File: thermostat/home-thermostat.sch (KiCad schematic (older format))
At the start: 35 parts, among them J1 SMA, SW1 SW_Push, U1 MKW41Z512VHT, Y1 32MHz, Y2 32,768KHz

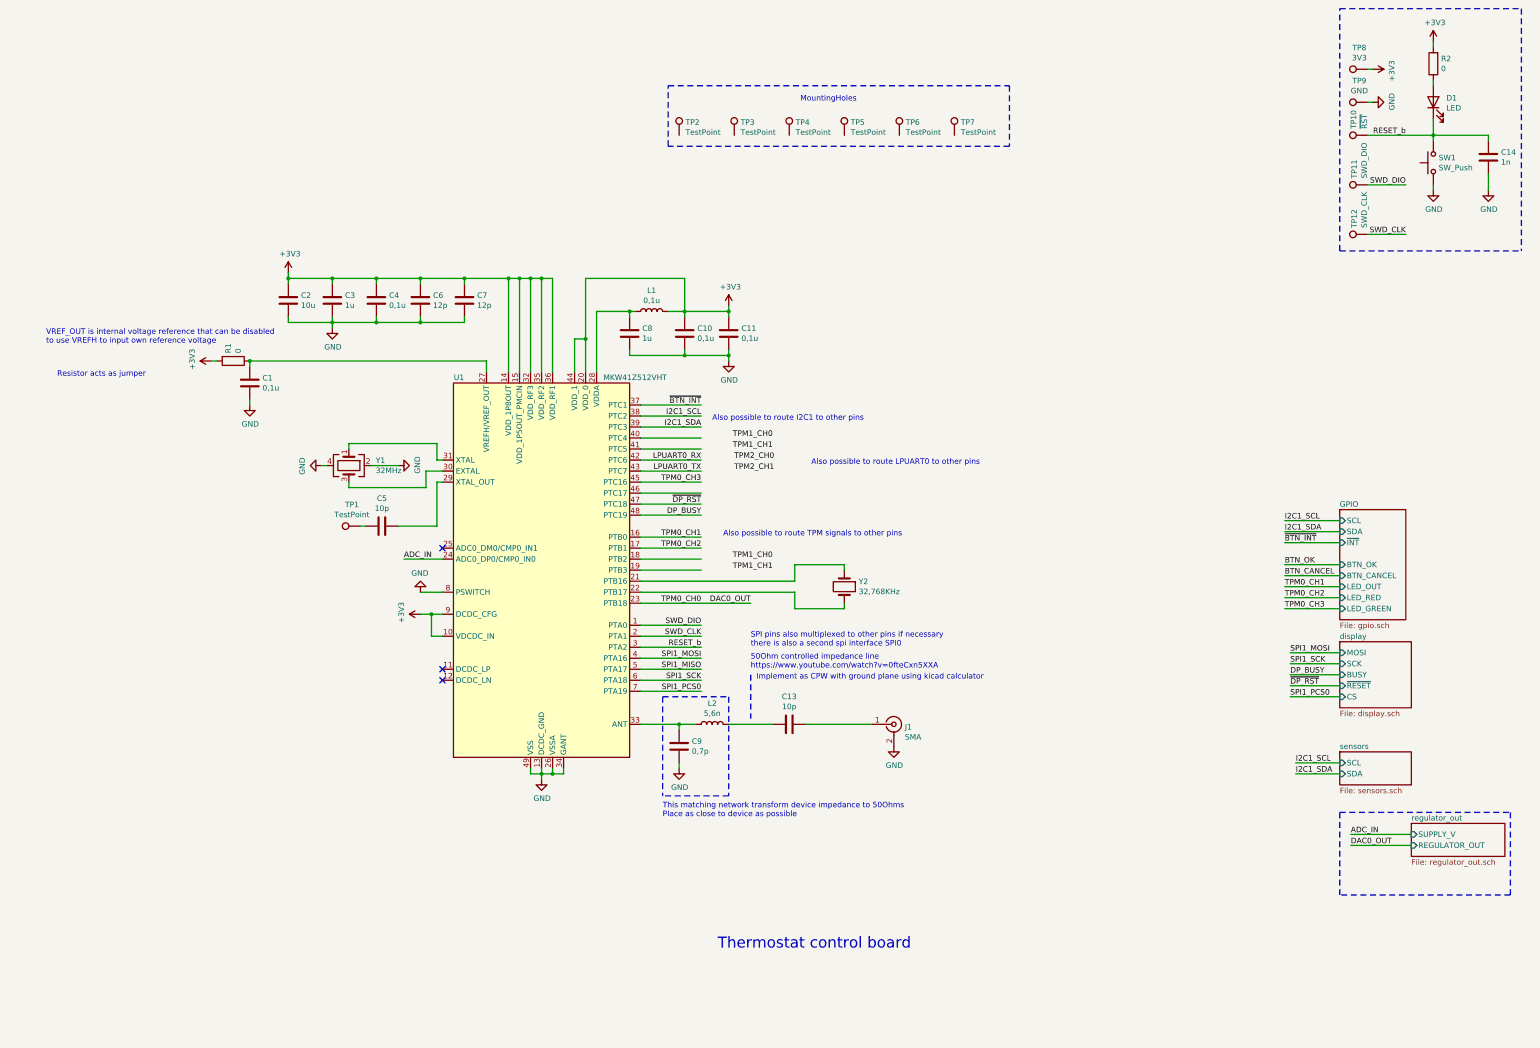
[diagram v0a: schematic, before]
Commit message: Finalized Thermostat circuit based on the MKW41Z.
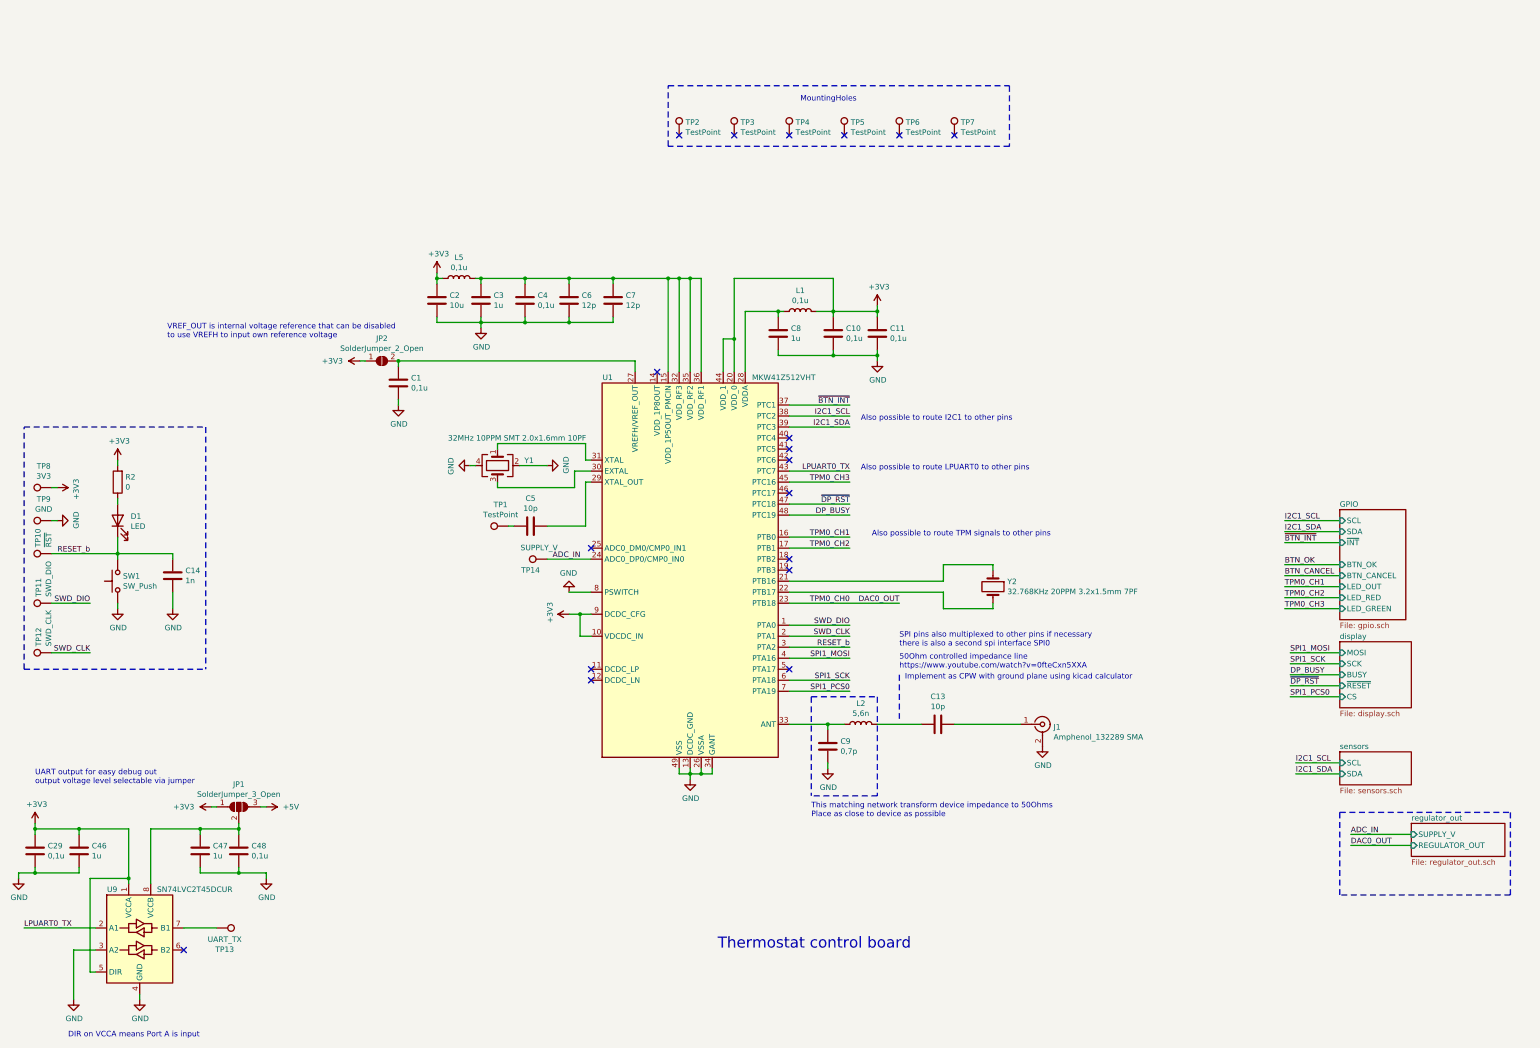
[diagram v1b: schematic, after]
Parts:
- removed R1: 0, Resistor_SMD:R_0603_1608Metric, symbol Device:R
- added C29, C48: 0,1u, Capacitor_SMD:C_0603_1608Metric, symbol Device:C
- added C46, C47: 1u, Capacitor_SMD:C_0603_1608Metric, symbol Device:C
- added JP1: SolderJumper_3_Open, Jumper:SolderJumper-3_P1.3mm_Open_Pad1.0x1.5mm, symbol Jumper:SolderJumper_3_Open
- added JP2: SolderJumper_2_Open, Jumper:SolderJumper-2_P1.3mm_Open_Pad1.0x1.5mm, symbol Jumper:SolderJumper_2_Open
- added L5: 0,1u, Inductor_SMD:L_0402_1005Metric, symbol Device:L
- added TP13: UART_TX, TestPoint:TestPoint_Pad_D1.0mm, symbol Connector:TestPoint
- added TP14: SUPPLY_V, TestPoint:TestPoint_Pad_D1.0mm, symbol Connector:TestPoint
- added U9: SN74LVC2T45DCUR, Package_SO:VSSOP-8_2.4x2.1mm_P0.5mm, symbol Logic_LevelTranslator:SN74LVC2T45DCUR
- C1, C10, C11, C13, C3, C4, C5, C6, C7, C9: footprint (none) -> Capacitor_SMD:C_0402_1005Metric
- C2, C8: footprint (none) -> Capacitor_SMD:C_0603_1608Metric
- J1: value SMA -> Amphenol_132289 SMA; footprint (none) -> Connector_Coaxial:SMA_Amphenol_132289_EdgeMount
- L1, L2: footprint (none) -> Inductor_SMD:L_0402_1005Metric
- U1: footprint Package_DFN_QFN:NXP_VQFN-48-1EP_7x7mm_P0.5mm_EP3.5x3.5mm_16xMask0.45x0.45_ThermalVias -> Package_DFN_QFN:NXP_LQFN-48-1EP_7x7mm_P0.5mm_EP3.5x3.5mm_16xMask0.45x0.45_ThermalVias
- Y1: value 32MHz -> 32MHz 10PPM SMT 2.0x1.6mm 10PF; footprint (none) -> Crystal:Crystal_SMD_2016-4Pin_2.0x1.6mm
- Y2: value 32,768KHz -> 32.768KHz 20PPM 3.2x1.5mm 7PF; footprint (none) -> Crystal:Crystal_SMD_3215-2Pin_3.2x1.5mm
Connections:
- net labels added: +5V
- net labels removed: LPUART0_RX, SPI1_MISO, TPM1_CH0, TPM1_CH1, TPM2_CH0, TPM2_CH1
- wire segments 151 -> 176
- no-connect marks 3 -> 18
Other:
- note added: "DIR on VCCA means Port A is input\n"
- note added: "UART output for easy debug out\noutput voltage level selectable via jumper"
- note removed: "Resistor acts as jumper"
- moved on the sheet: C1, C10, C11, C13, C14, C2, C3, C4, C5, C6, C7, C8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

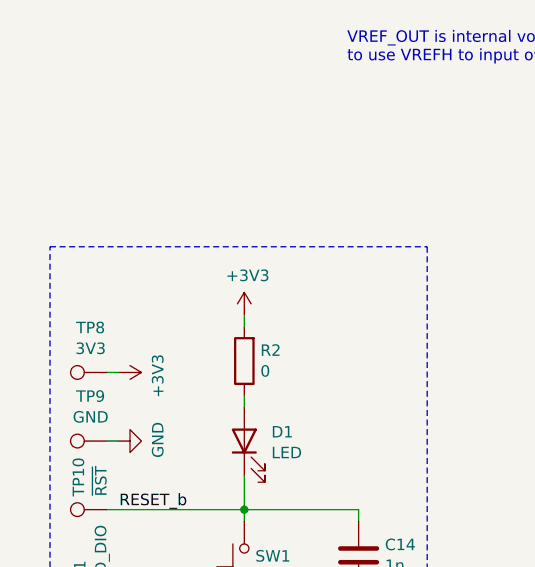
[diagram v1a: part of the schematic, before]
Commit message: Added testpad to supply rail +5V to allow flexible powering of board,also over Arduino.
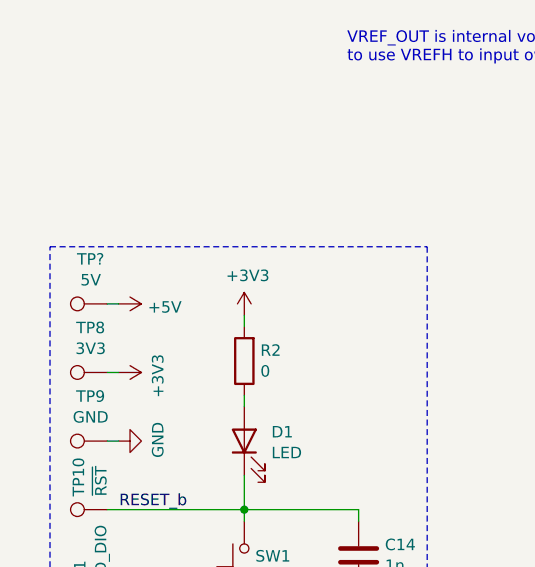
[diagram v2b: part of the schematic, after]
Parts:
- added TP?: 5V, TestPoint:TestPoint_Pad_D1.0mm, symbol Connector:TestPoint
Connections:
- net +5V: now also TP?.1
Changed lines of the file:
@@
 Wire Wire Line
 	5450 3350 5850 3350
+$Comp
+L Connector:TestPoint TP?
+U 1 1 5F6F1851
+P 950 2400
+F 0 "TP?" V 1145 2472 50  0000 C CNN
+F 1 "5V" V 1054 2472 50  0000 C CNN
+F 2 "TestPoint:TestPoint_Pad_D1.0mm" H 1150 2400 50  0001 C CNN
+F 3 "~" H 1150 2400 50  0001 C CNN
+	1    950  2400
+	0    -1   -1   0
+$EndComp
+$Comp
+L power:+5V #PWR?
+U 1 1 5F6F2232
+P 1000 2400
+F 0 "#PWR?" H 1000 2250 50  0001 C CNN
+F 1 "+5V" V 1015 2528 50  0000 L CNN
+F 2 "" H 1000 2400 50  0001 C CNN
+F 3 "" H 1000 2400 50  0001 C CNN
+	1    1000 2400
+	0    1    1    0
+$EndComp
+Wire Wire Line
+	1000 2400 950  2400
 $EndSCHEMATC

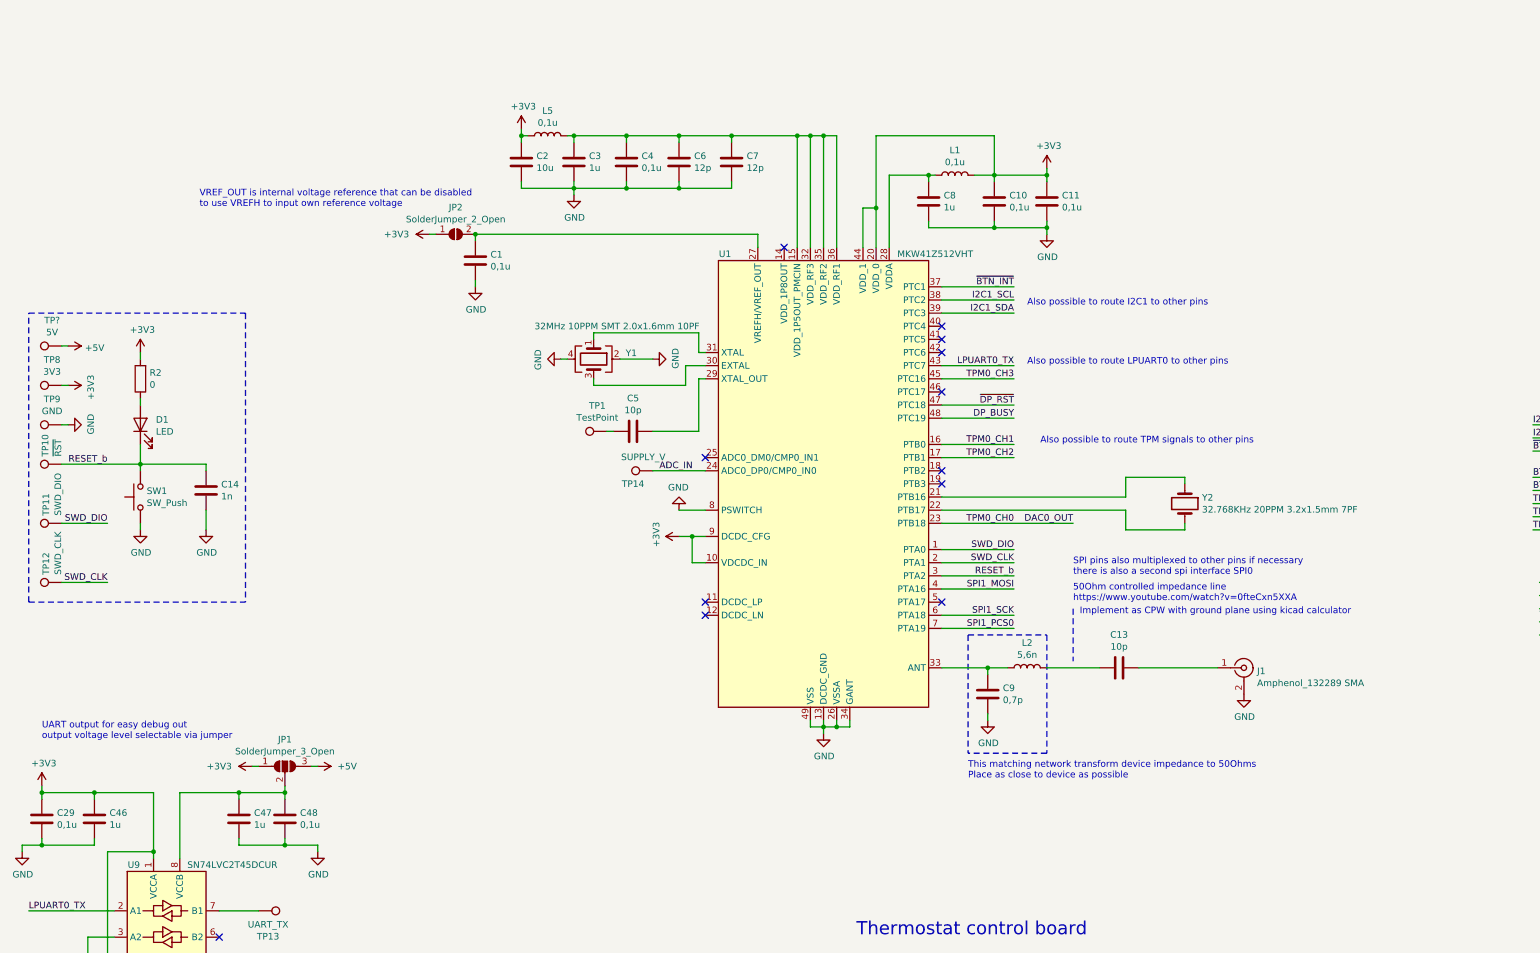
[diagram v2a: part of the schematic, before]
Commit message: Started grouping footprints on PCB, configured minimal via and trace sizes for PCB_POOL.
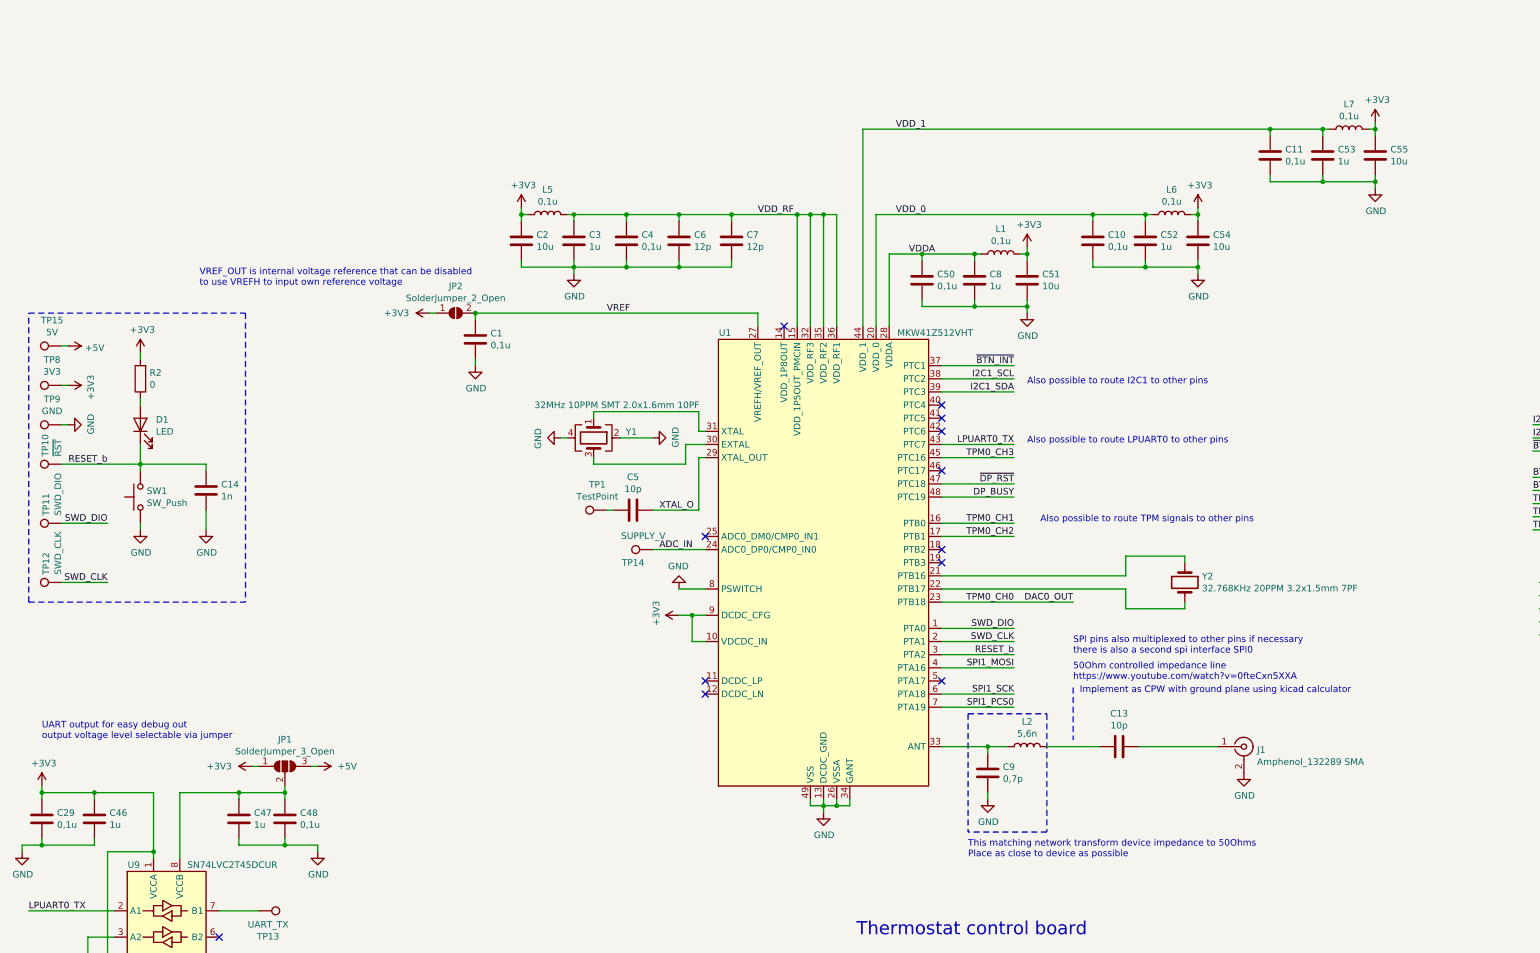
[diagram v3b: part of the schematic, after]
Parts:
- added C50: 0,1u, Capacitor_SMD:C_0402_1005Metric, symbol Device:C
- added C51, C54, C55: 10u, Capacitor_SMD:C_0603_1608Metric, symbol Device:C
- added C52, C53: 1u, Capacitor_SMD:C_0402_1005Metric, symbol Device:C
- added L6, L7: 0,1u, Inductor_SMD:L_0402_1005Metric, symbol Device:L
- C8: footprint Capacitor_SMD:C_0603_1608Metric -> Capacitor_SMD:C_0402_1005Metric
- gave numbers to parts that had none: 1
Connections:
- net +3V3: now also C51.2, C54.2, C55.2, L6.2, L7.2; no longer C10.1, C11.1, U1.20 (VDD_0), U1.44 (VDD_1)
- net GND: now also C50.2, C51.1, C52.2, C53.2, C54.1, C55.1
- net VDD_RF: now reaches C3.1, C4.1, C6.1, C7.1, L5.2, U1.15 (VDD_1P5OUT_PMCIN), U1.32 (VDD_RF3), U1.35 (VDD_RF2), U1.36 (VDD_RF1)
- net VREF: now reaches C1.1, JP2.2 (B), U1.27 (VREFH/VREF_OUT)
- net VDDA: now reaches C8.1, L1.1, U1.28 (VDDA)
- net VDDA: now also C50.1
- net XTAL_O: now reaches C5.1, U1.29 (XTAL_OUT)
- new net VDD_0: C10.1, C52.1, L6.1, U1.20 (VDD_0)
- new net VDD_1: C11.1, C53.1, L7.1, U1.44 (VDD_1)
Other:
- moved on the sheet: C1, C10, C11, C13, C2, C3, C4, C5, C6, C7, C8, C9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

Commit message: Removed buttons and signal LEDs as they should be moved to a separate peripheral board (to save expensive board space on the 4-layer PCB). Added bus transceiver for UART_RX to optionally be able to accept inputs over UART.
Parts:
- removed D1: LED, LED_SMD:LED_1210_3225Metric, symbol Device:LED
- removed SW1: SW_Push, Button_Switch_SMD:SW_SPST_Panasonic_EVQPL_3PL_5PL_PT_A08, symbol Switch:SW_Push
- removed TP10: ~RST, TestPoint:TestPoint_Pad_D1.0mm, symbol Connector:TestPoint
- removed TP11: SWD_DIO, TestPoint:TestPoint_Pad_D1.0mm, symbol Connector:TestPoint
- removed TP12: SWD_CLK, TestPoint:TestPoint_Pad_D1.0mm, symbol Connector:TestPoint
- removed TP6, TP7: TestPoint, MountingHole:MountingHole_3.2mm_M3, symbol Connector:TestPoint
- added C56, C59: 0,1u, Capacitor_SMD:C_0603_1608Metric, symbol Device:C
- added C57, C58: 1u, Capacitor_SMD:C_0603_1608Metric, symbol Device:C
- added J4: Conn_ARM_JTAG_SWD_10, Connector_PinHeader_1.27mm:PinHeader_2x05_P1.27mm_Vertical_SMD, symbol Connector:Conn_ARM_JTAG_SWD_10
- added TP16: UART_RX, TestPoint:TestPoint_Pad_D1.0mm, symbol Connector:TestPoint
- added U10: SN74LVC2T45DCUR, Package_SO:VSSOP-8_2.4x2.1mm_P0.5mm, symbol Logic_LevelTranslator:SN74LVC2T45DCUR
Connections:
- net +3V3: now also C56.1, C57.1, J4.1 (VTref), U10.1 (VCCA)
- net GND: now also C56.2, C57.2, C58.2, C59.2, J4.3 (GND), J4.5 (GND), J4.9 (GNDDetect), U10.4 (GND), U10.5 (DIR), U10.6 (B2)
- net RESET_b: now also R2.1, J4.10 (~RESET~)
- net SWD_CLK: now also J4.4 (SWDCLK/TCK)
- net SWD_DIO: now also J4.2 (SWDIO/TMS)
- net LPUART0_RX: now reaches U1.42 (PTC6)
- net LPUART0_RX: now also U10.2 (A1)
- net at C47.1, C48.1, JP1.2 (C)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: now also C58.1, C59.1, U10.8 (VCCB)
- new net: TP16.1, U10.7 (B1)
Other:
- note added: "DIR on GND means Port A is output"
- note added: "UART for easy debug\noutput voltage level selectable via jumper"
- note removed: "UART output for easy debug out\noutput voltage level selectable via jumper"
- moved on the sheet: C14, C29, C46, C47, C48, JP1, R2, TP13, TP9, U9
